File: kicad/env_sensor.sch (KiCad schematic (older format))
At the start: 6 parts, among them IC1 VEML7700-TT, J12 WEATHER_I2C, Q3 DTC113Z, U1 HDC2010YPAT

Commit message: Libraries cleanup
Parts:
- IC1: footprint SamacSys:VEML7700 -> SamacSys_Parts:VEML7700; symbol SamaSys:VEML7700-TT -> SamacSys_Parts:VEML7700-TT
- U1: footprint LocalsLib:BGA6C100X50P2X3_146X146X67 -> Parts:BGA6C100X50P2X3_146X146X67; symbol HDC2010YPAT:HDC2010YPAT -> Parts:HDC2010YPAT
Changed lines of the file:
@@
 $Descr A4 11693 8268
 encoding utf-8
-Sheet 4 6
+Sheet 4 7
 Title ""
 Date ""
@@
 I2C ADDR 0x10
 $Comp
-L SamaSys:VEML7700-TT IC?
+L SamacSys_Parts:VEML7700-TT IC?
 U 1 1 605F5D4E
 P 7350 3250
@@
 F 0 "IC1" V 7900 3150 50  0000 R CNN
 F 1 "VEML7700-TT" H 8050 2800 50  0000 R CNN
-F 2 "SamacSys:VEML7700" H 8100 3350 50  0001 L CNN
+F 2 "SamacSys_Parts:VEML7700" H 8100 3350 50  0001 L CNN
 F 3 "https://www.arrow.com/en/products/veml7700-tt/vishay" H 8100 3250 50  0001 L CNN
 F 4 "16Bit Ambient Light Sensor I2C 6.8x2.3mm" H 8100 3150 50  0001 L CNN "Description"
@@
 I2C ADDR 0x40
 $Comp
-L HDC2010YPAT:HDC2010YPAT U?
+L Parts:HDC2010YPAT U?
 U 1 1 605F5D91
 P 5000 3050
@@
 F 0 "U1" H 5000 3000 50  0000 C CNN
 F 1 "HDC2010YPAT" H 5050 2800 50  0000 C CNN
-F 2 "LocalsLib:BGA6C100X50P2X3_146X146X67" H 5000 3050 50  0001 L BNN
+F 2 "Parts:BGA6C100X50P2X3_146X146X67" H 5000 3050 50  0001 L BNN
 F 3 "Texas Instruments" H 5000 3050 50  0001 L BNN
 F 4 "0.675 mm" H 5000 3050 50  0001 L BNN "Field4"

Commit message: Comitting yesterday's leftovers
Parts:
- renumbered C14 to C10, C13 to C9, IC1 to IC3, J12 to J9, Q3 to Q2, U1 to U4
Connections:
- net GNDA: no longer C10.2, C9.2, IC3.3 (GND), Q2.3 (C), U4.C1 (GND)
- net VDD renamed +3V3
- new net GND_S: C10.2, C9.2, IC3.3 (GND), Q2.3 (C), U4.C1 (GND)
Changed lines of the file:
@@
 P 7350 3250
 AR Path="/605F5D4E" Ref="IC?"  Part="1"
-AR Path="/605E9160/605F5D4E" Ref="IC1"  Part="1"
-F 0 "IC1" V 7900 3150 50  0000 R CNN
+AR Path="/605E9160/605F5D4E" Ref="IC3"  Part="1"
+F 0 "IC3" V 7900 3150 50  0000 R CNN
 F 1 "VEML7700-TT" H 8050 2800 50  0000 R CNN
 F 2 "SamacSys_Parts:VEML7700" H 8100 3350 50  0001 L CNN
@@
 AR Path="/60DE59F5/605F5D54" Ref="#PWR?"  Part="1"
 AR Path="/605F5D54" Ref="#PWR?"  Part="1"
-AR Path="/605E9160/605F5D54" Ref="#PWR035"  Part="1"
-F 0 "#PWR035" H 6700 3650 50  0001 C CNN
+AR Path="/605E9160/605F5D54" Ref="#PWR047"  Part="1"
+F 0 "#PWR047" H 6700 3650 50  0001 C CNN
 F 1 "GND" V 6700 3700 50  0000 C CNN
 F 2 "" H 6700 3900 50  0001 C CNN
@@
 AR Path="/60DE59F5/605F5D6D" Ref="C?"  Part="1"
 AR Path="/605F5D6D" Ref="C?"  Part="1"
-AR Path="/605E9160/605F5D6D" Ref="C14"  Part="1"
-F 0 "C14" H 6550 3200 50  0000 L CNN
+AR Path="/605E9160/605F5D6D" Ref="C10"  Part="1"
+F 0 "C10" H 6550 3200 50  0000 L CNN
 F 1 "0.1μF" H 6550 3000 50  0000 L CNN
 F 2 "Capacitor_SMD:C_1206_3216Metric" H 6538 2950 50  0001 C CNN
@@
 P 6600 3700
 AR Path="/605F5D73" Ref="Q?"  Part="1"
-AR Path="/605E9160/605F5D73" Ref="Q3"  Part="1"
-F 0 "Q3" V 6450 3450 50  0000 C CNN
-F 1 "DTC113Z" V 6550 3350 50  0000 C CNN
+AR Path="/605E9160/605F5D73" Ref="Q2"  Part="1"
+F 0 "Q2" H 6400 3500 50  0000 C CNN
+F 1 "DTC113Z" H 6400 3400 50  0000 C CNN
 F 2 "Parts:DTC113ZEBTL" H 6600 3700 50  0001 L CNN
 F 3 "" H 6600 3700 50  0001 L CNN
@@
 P 5000 3050
 AR Path="/605F5D91" Ref="U?"  Part="1"
-AR Path="/605E9160/605F5D91" Ref="U1"  Part="1"
-F 0 "U1" H 5000 3000 50  0000 C CNN
+AR Path="/605E9160/605F5D91" Ref="U4"  Part="1"
+F 0 "U4" H 5000 3000 50  0000 C CNN
 F 1 "HDC2010YPAT" H 5050 2800 50  0000 C CNN
 F 2 "Parts:BGA6C100X50P2X3_146X146X67" H 5000 3050 50  0001 L BNN
@@
 	1    0    0    -1
 $EndComp
-Text Label 6300 3700 3    50   ~ 0
+Text Label 6300 3700 2    50   ~ 0
 ALL_EN
 Wire Wire Line
@@
 P 8700 3200
 AR Path="/605F5DA7" Ref="#PWR?"  Part="1"
-AR Path="/605E9160/605F5DA7" Ref="#PWR037"  Part="1"
-F 0 "#PWR037" H 8700 2950 50  0001 C CNN
+AR Path="/605E9160/605F5DA7" Ref="#PWR044"  Part="1"
+F 0 "#PWR044" H 8700 2950 50  0001 C CNN
 F 1 "GND" V 8705 3072 50  0000 R CNN
 F 2 "" H 8700 3200 50  0001 C CNN
@@
 P 8700 3200
 AR Path="/605F5DC5" Ref="J?"  Part="1"
-AR Path="/605E9160/605F5DC5" Ref="J12"  Part="1"
-F 0 "J12" H 9150 3465 50  0000 C CNN
+AR Path="/605E9160/605F5DC5" Ref="J9"  Part="1"
+F 0 "J9" H 9150 3465 50  0000 C CNN
 F 1 "WEATHER_I2C" H 9150 3374 50  0000 C CNN
 F 2 "Parts:Molex_Conn_SMD_01x06_505567_0671" H 9450 3300 50  0001 L CNN
@@
 	6700 3450 7350 3450
 Connection ~ 6700 3450
-Wire Wire Line
-	5700 3450 6350 3450
 NoConn ~ 8700 3600
-Text Label 5900 3450 0    50   ~ 0
+$Comp
+L Device:C C9
+U 1 1 5FCEC376
+P 6200 3100
+F 0 "C9" H 6050 3200 50  0000 L CNN
+F 1 "4.7uF" H 5950 3000 50  0000 L CNN
+F 2 "Capacitor_SMD:C_1206_3216Metric" H 6238 2950 50  0001 C CNN
+F 3 "~" H 6200 3100 50  0001 C CNN
+	1    6200 3100
+	1    0    0    -1
+$EndComp
+Text Label 4300 2950 2    50   ~ 0
 GNDA
 $Comp
-L power:VDD #PWR058
-U 1 1 5FA64890
+L power:+3.3V #PWR045
+U 1 1 6115FE3E
 P 8700 3300
-F 0 "#PWR058" H 8700 3150 50  0001 C CNN
-F 1 "VDD" V 8715 3427 50  0000 L CNN
+F 0 "#PWR045" H 8700 3150 50  0001 C CNN
+F 1 "+3.3V" V 8715 3428 50  0000 L CNN
 F 2 "" H 8700 3300 50  0001 C CNN
 F 3 "" H 8700 3300 50  0001 C CNN
@@
 	0    -1   -1   0
 $EndComp
-Wire Wire Line
-	6200 2850 6350 2850
-$Comp
-L power:VDD #PWR056
-U 1 1 5FA66E92
-P 6350 2850
-F 0 "#PWR056" H 6350 2700 50  0001 C CNN
-F 1 "VDD" H 6365 3023 50  0000 C CNN
-F 2 "" H 6350 2850 50  0001 C CNN
-F 3 "" H 6350 2850 50  0001 C CNN
-	1    6350 2850
-	1    0    0    -1
-$EndComp
-Connection ~ 6350 2850
-Wire Wire Line
-	6350 2850 6500 2850
-$Comp
-L power:VDD #PWR055
-U 1 1 5FA697CD
-P 5700 2750
-F 0 "#PWR055" H 5700 2600 50  0001 C CNN
-F 1 "VDD" V 5715 2878 50  0000 L CNN
-F 2 "" H 5700 2750 50  0001 C CNN
-F 3 "" H 5700 2750 50  0001 C CNN
-	1    5700 2750
-	0    1    1    0
-$EndComp
-$Comp
-L power:VDD #PWR057
-U 1 1 5FA6A4C8
+$Comp
+L power:+3.3V #PWR046
+U 1 1 61160588
 P 7350 3350
-F 0 "#PWR057" H 7350 3200 50  0001 C CNN
-F 1 "VDD" V 7365 3477 50  0000 L CNN
+F 0 "#PWR046" H 7350 3200 50  0001 C CNN
+F 1 "+3.3V" V 7365 3478 50  0000 L CNN
 F 2 "" H 7350 3350 50  0001 C CNN
 F 3 "" H 7350 3350 50  0001 C CNN
@@
 $EndComp
 $Comp
-L Device:C C13
-U 1 1 5FCEC376
-P 6200 3100
-F 0 "C13" H 6050 3200 50  0000 L CNN
-F 1 "4.7uF" H 5950 3000 50  0000 L CNN
-F 2 "Capacitor_SMD:C_1206_3216Metric" H 6238 2950 50  0001 C CNN
-F 3 "~" H 6200 3100 50  0001 C CNN
-	1    6200 3100
-	1    0    0    -1
-$EndComp
-Text Label 4300 2950 2    50   ~ 0
-GNDA
+L power:+3.3V #PWR043
+U 1 1 61160CBD
+P 6350 2650
+F 0 "#PWR043" H 6350 2500 50  0001 C CNN
+F 1 "+3.3V" H 6365 2823 50  0000 C CNN
+F 2 "" H 6350 2650 50  0001 C CNN
+F 3 "" H 6350 2650 50  0001 C CNN
+	1    6350 2650
+	1    0    0    -1
+$EndComp
+Wire Wire Line
+	6200 2850 6350 2850
+Wire Wire Line
+	6350 2650 6350 2750
+Connection ~ 6350 2850
+Wire Wire Line
+	6350 2850 6500 2850
+Wire Wire Line
+	5700 2750 6350 2750
+Connection ~ 6350 2750
+Wire Wire Line
+	6350 2750 6350 2850
+Wire Wire Line
+	5700 3450 6350 3450
+$Comp
+L power:PWR_FLAG #FLG03
+U 1 1 61239139
+P 6700 3450
+F 0 "#FLG03" H 6700 3525 50  0001 C CNN
+F 1 "PWR_FLAG" H 6700 3623 50  0000 C CNN
+F 2 "" H 6700 3450 50  0001 C CNN
+F 3 "~" H 6700 3450 50  0001 C CNN
+	1    6700 3450
+	1    0    0    -1
+$EndComp
+Text Label 5900 3450 0    50   ~ 0
+GND_S
 $EndSCHEMATC

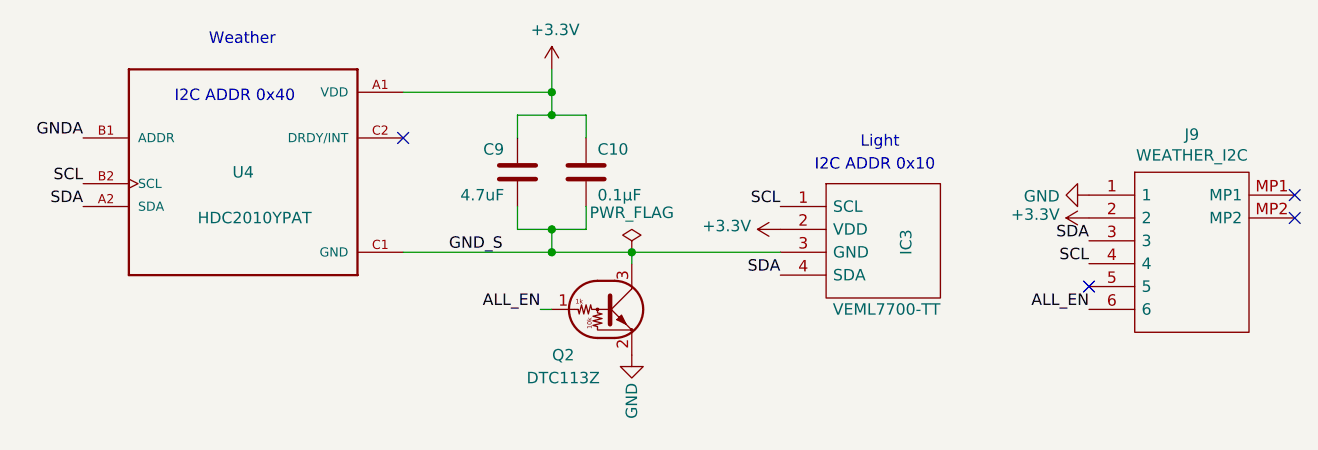
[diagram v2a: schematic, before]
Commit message: Mapped footprints, PCB in progress
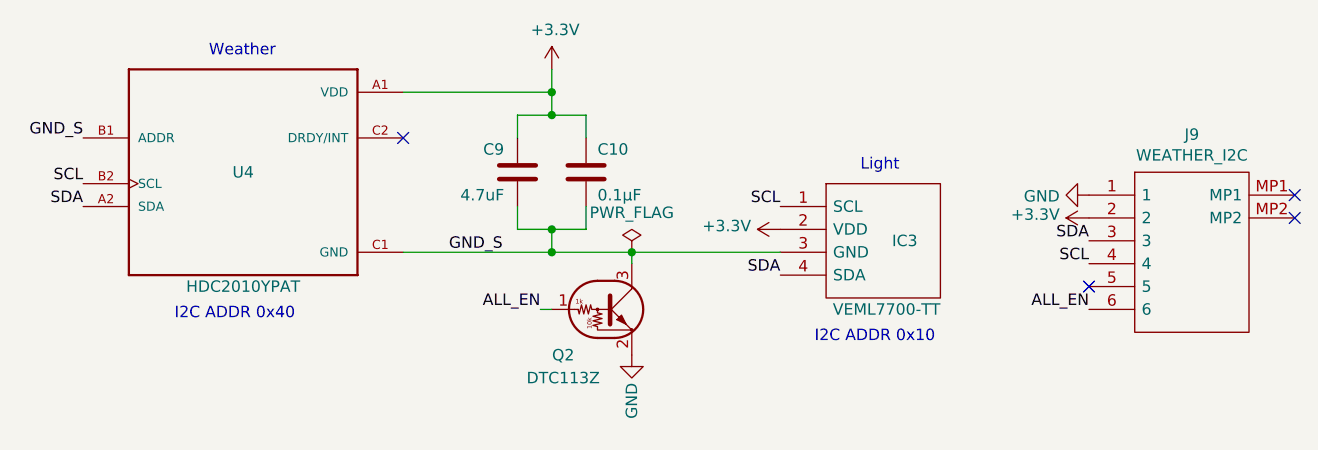
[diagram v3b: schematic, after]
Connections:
- net GNDA is gone; now on net GND_S: U4.B1 (ADDR)
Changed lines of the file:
@@
 Wire Wire Line
 	6350 3700 6300 3700
-Text Notes 7700 3000 0    50   ~ 0
+Text Notes 7700 3100 0    50   ~ 0
 Light
 Text Label 7350 3550 2    50   ~ 0
@@
 Text Label 7350 3250 2    50   ~ 0
 SCL
-Text Notes 7500 3100 0    50   ~ 0
+Text Notes 7500 3850 0    50   ~ 0
 I2C ADDR 0x10
 $Comp
@@
 AR Path="/605F5D4E" Ref="IC?"  Part="1"
 AR Path="/605E9160/605F5D4E" Ref="IC3"  Part="1"
-F 0 "IC3" V 7900 3150 50  0000 R CNN
+F 0 "IC3" H 7950 3100 50  0000 R CNN
 F 1 "VEML7700-TT" H 8050 2800 50  0000 R CNN
 F 2 "SamacSys_Parts:VEML7700" H 8100 3350 50  0001 L CNN
@@
 	6350 3350 6500 3350
 NoConn ~ 5700 2950
-Text Notes 4850 2550 0    50   ~ 0
+Text Notes 4850 2600 0    50   ~ 0
 Weather
 Text Label 4300 3150 2    50   ~ 0
@@
 Text Label 4300 3250 2    50   ~ 0
 SDA
-Text Notes 4700 2800 0    50   ~ 0
+Text Notes 4700 3750 0    50   ~ 0
 I2C ADDR 0x40
-$Comp
-L Parts:HDC2010YPAT U?
-U 1 1 605F5D91
-P 5000 3050
-AR Path="/605F5D91" Ref="U?"  Part="1"
-AR Path="/605E9160/605F5D91" Ref="U4"  Part="1"
-F 0 "U4" H 5000 3000 50  0000 C CNN
-F 1 "HDC2010YPAT" H 5050 2800 50  0000 C CNN
-F 2 "Parts:BGA6C100X50P2X3_146X146X67" H 5000 3050 50  0001 L BNN
-F 3 "Texas Instruments" H 5000 3050 50  0001 L BNN
-F 4 "0.675 mm" H 5000 3050 50  0001 L BNN "Field4"
-F 5 "C" H 5000 3050 50  0001 L BNN "Field5"
-F 6 "IPC 7351B" H 5000 3050 50  0001 L BNN "Field6"
-	1    5000 3050
-	1    0    0    -1
-$EndComp
 Text Label 6300 3700 2    50   ~ 0
 ALL_EN
@@
 $EndComp
 Text Label 4300 2950 2    50   ~ 0
-GNDA
+GND_S
 $Comp
 L power:+3.3V #PWR045
@@
 Text Label 5900 3450 0    50   ~ 0
 GND_S
+$Comp
+L Parts:HDC2010YPAT U?
+U 1 1 605F5D91
+P 5000 3050
+AR Path="/605F5D91" Ref="U?"  Part="1"
+AR Path="/605E9160/605F5D91" Ref="U4"  Part="1"
+F 0 "U4" H 5000 3000 50  0000 C CNN
+F 1 "HDC2010YPAT" H 5000 2500 50  0000 C CNN
+F 2 "Parts:BGA6C100X50P2X3_146X146X67" H 5000 3050 50  0001 L BNN
+F 3 "Texas Instruments" H 5000 3050 50  0001 L BNN
+F 4 "0.675 mm" H 5000 3050 50  0001 L BNN "Field4"
+F 5 "C" H 5000 3050 50  0001 L BNN "Field5"
+F 6 "IPC 7351B" H 5000 3050 50  0001 L BNN "Field6"
+	1    5000 3050
+	1    0    0    -1
+$EndComp
 $EndSCHEMATC
